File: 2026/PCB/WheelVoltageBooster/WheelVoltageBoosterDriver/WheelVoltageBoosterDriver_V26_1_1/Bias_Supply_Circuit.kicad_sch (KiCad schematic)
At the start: 27 parts, among them U1 MAX20405AFOA/VY+, U5 LD1117DT33CTR

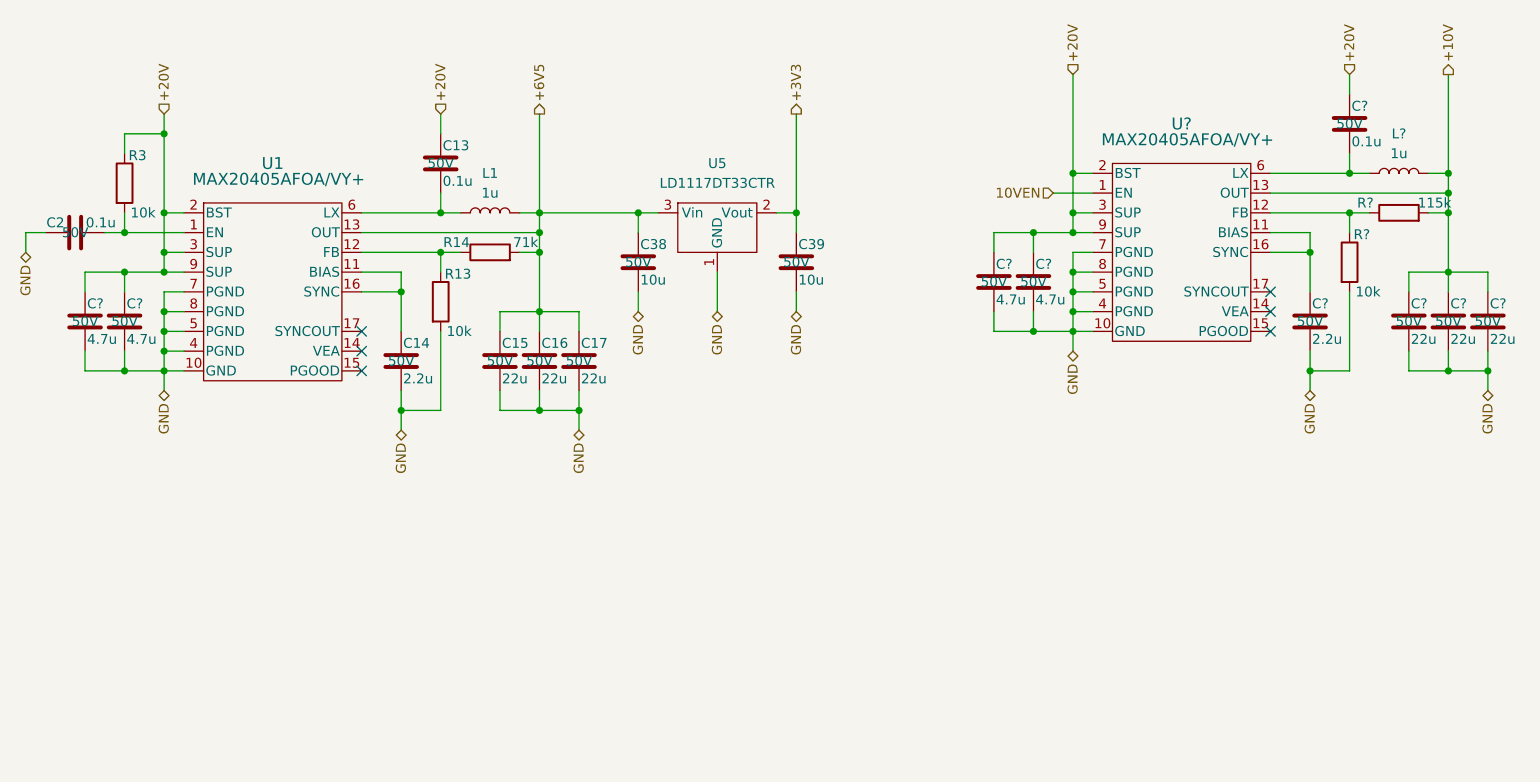
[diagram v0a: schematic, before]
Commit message: ５０V 測定用分圧抵抗追加
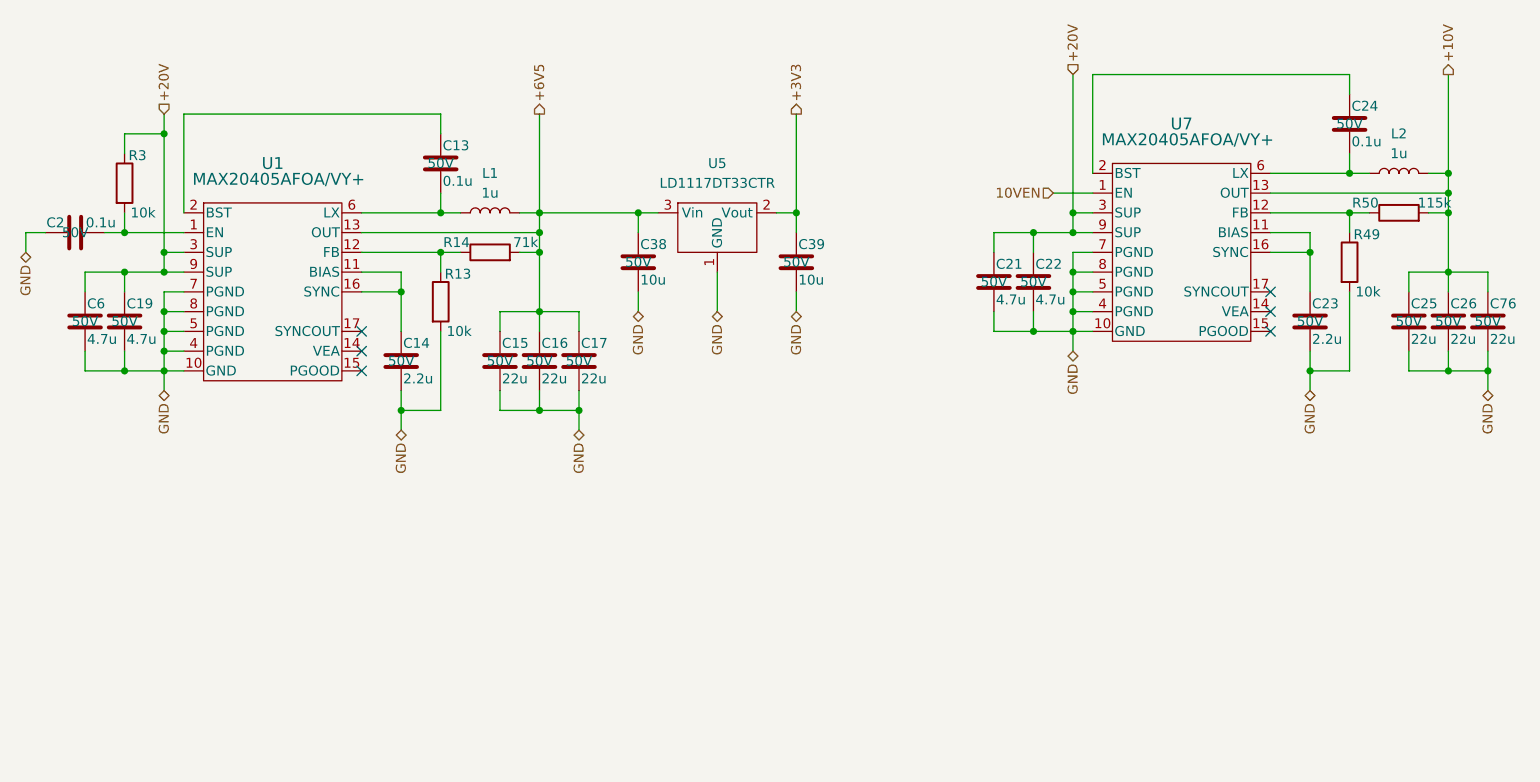
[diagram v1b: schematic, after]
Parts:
- gave numbers to parts that had none: 13
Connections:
- net +20V: no longer C13.1, C24.1, U1.2 (BST), U7.2 (BST)
- new net: C24.1, U7.2 (BST)
- new net: C13.1, U1.2 (BST)
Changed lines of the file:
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@@
 	)
 	(junction
-		(at 179.07 78.74)
-		(diameter 0)
-		(color 0 0 0 0)
-	)
-	(junction
 		(at 209.55 104.14)
 		(diameter 0)
@@
 	)
 	(junction
-		(at 62.23 83.82)
-		(diameter 0)
-		(color 0 0 0 0)
-	)
-	(junction
 		(at 227.33 81.28)
 		(diameter 0)
@@
 	(wire
 		(pts
-			(xy 179.07 66.04) (xy 179.07 78.74)
-		)
-		(stroke
-			(width 0)
-			(type default)
-		)
-	)
-	(wire
-		(pts
-			(xy 179.07 78.74) (xy 181.61 78.74)
-		)
-		(stroke
-			(width 0)
-			(type default)
-		)
-	)
-	(wire
-		(pts
 			(xy 115.57 106.68) (xy 115.57 109.22)
 		)
@@
 	(wire
 		(pts
-			(xy 179.07 78.74) (xy 179.07 83.82)
+			(xy 179.07 66.04) (xy 179.07 83.82)
 		)
 		(stroke
@@
 	(wire
 		(pts
+			(xy 181.61 66.04) (xy 214.63 66.04)
+		)
+		(stroke
+			(width 0)
+			(type default)
+		)
+	)
+	(wire
+		(pts
 			(xy 176.53 81.28) (xy 181.61 81.28)
 		)
@@
 	(wire
 		(pts
+			(xy 64.77 83.82) (xy 64.77 71.12)
+		)
+		(stroke
+			(width 0)
+			(type default)
+		)
+	)
+	(wire
+		(pts
 			(xy 110.49 83.82) (xy 123.19 83.82)
 		)
@@
 	(wire
 		(pts
-			(xy 62.23 83.82) (xy 64.77 83.82)
+			(xy 204.47 81.28) (xy 227.33 81.28)
 		)
 		(stroke
@@
 	(wire
 		(pts
-			(xy 204.47 81.28) (xy 227.33 81.28)
+			(xy 181.61 78.74) (xy 181.61 66.04)
 		)
 		(stroke
@@
 	(wire
 		(pts
-			(xy 62.23 83.82) (xy 62.23 88.9)
+			(xy 62.23 73.66) (xy 62.23 88.9)
 		)
 		(stroke
@@
 	(wire
 		(pts
-			(xy 52.07 93.98) (xy 52.07 91.44)
+			(xy 64.77 71.12) (xy 97.79 71.12)
 		)
 		(stroke
@@
 	(wire
 		(pts
-			(xy 227.33 78.74) (xy 224.79 78.74)
+			(xy 52.07 93.98) (xy 52.07 91.44)
 		)
 		(stroke
@@
 	(wire
 		(pts
-			(xy 179.07 93.98) (xy 179.07 91.44)
+			(xy 227.33 78.74) (xy 224.79 78.74)
 		)
 		(stroke
@@
 	(wire
 		(pts
-			(xy 123.19 83.82) (xy 123.19 86.36)
+			(xy 179.07 93.98) (xy 179.07 91.44)
 		)
 		(stroke
@@
 	(wire
 		(pts
-			(xy 140.97 83.82) (xy 143.51 83.82)
+			(xy 123.19 83.82) (xy 123.19 86.36)
 		)
 		(stroke
@@
 	(wire
 		(pts
-			(xy 62.23 73.66) (xy 62.23 83.82)
+			(xy 140.97 83.82) (xy 143.51 83.82)
 		)
 		(stroke
@@
 		)
 	)
-	(hierarchical_label "+20V"
-		(shape input)
-		(at 214.63 66.04 90)
-		(effects
-			(font
-				(size 1.27 1.27)
-			)
-			(justify left)
-		)
-	)
-	(hierarchical_label "+20V"
-		(shape input)
-		(at 97.79 71.12 90)
-		(effects
-			(font
-				(size 1.27 1.27)
-			)
-			(justify left)
-		)
-	)
 	(hierarchical_label "GND"
 		(shape bidirectional)
@@
 		(on_board yes)
 		(dnp no)
-		(property "Reference" "C?"
+		(property "Reference" "C25"
 			(at 222.504 95.504 0)
 			(effects
@@
 			(project "WheelVoltageBoosterDriver_V26_1_1"
 				(path "/80c9ed4f-d051-48b1-8382-19040773b73e/6c235b48-13ab-434e-8894-09a09ebdd0ec"
-					(reference "C?")
+					(reference "C25")
 					(unit 1)
 				)
@@
 		(on_board yes)
 		(dnp no)
-		(property "Reference" "R?"
+		(property "Reference" "R49"
 			(at 215.138 86.614 0)
 			(effects
@@
 			(project "WheelVoltageBoosterDriver_V26_1_1"
 				(path "/80c9ed4f-d051-48b1-8382-19040773b73e/6c235b48-13ab-434e-8894-09a09ebdd0ec"
-					(reference "R?")
+					(reference "R49")
 					(unit 1)
 				)
@@
 		(on_board yes)
 		(dnp no)
-		(property "Reference" "U?"
+		(property "Reference" "U7"
 			(at 193.04 72.39 0)
 			(effects
@@
 			(project "WheelVoltageBoosterDriver_V26_1_1"
 				(path "/80c9ed4f-d051-48b1-8382-19040773b73e/6c235b48-13ab-434e-8894-09a09ebdd0ec"
-					(reference "U?")
+					(reference "U7")
 					(unit 1)
 				)
@@
 		(dnp no)
 		(fields_autoplaced yes)
-		(property "Reference" "L?"
+		(property "Reference" "L2"
 			(at 220.98 73.66 90)
 			(effects
@@
 			(project "WheelVoltageBoosterDriver_V26_1_1"
 				(path "/80c9ed4f-d051-48b1-8382-19040773b73e/6c235b48-13ab-434e-8894-09a09ebdd0ec"
-					(reference "L?")
+					(reference "L2")
 					(unit 1)
 				)
@@
 		(on_board yes)
 		(dnp no)
-		(property "Reference" "C?"
+		(property "Reference" "C19"
 			(at 57.404 95.504 0)
 			(effects
@@
 			(project "WheelVoltageBoosterDriver_V26_1_1"
 				(path "/80c9ed4f-d051-48b1-8382-19040773b73e/6c235b48-13ab-434e-8894-09a09ebdd0ec"
-					(reference "C?")
+					(reference "C19")
 					(unit 1)
 				)
@@
 		(on_board yes)
 		(dnp no)
-		(property "Reference" "C?"
+		(property "Reference" "C24"
 			(at 214.884 70.104 0)
 			(effects
@@
 			(project "WheelVoltageBoosterDriver_V26_1_1"
 				(path "/80c9ed4f-d051-48b1-8382-19040773b73e/6c235b48-13ab-434e-8894-09a09ebdd0ec"
-					(reference "C?")
+					(reference "C24")
 					(unit 1)
 				)
@@
 		(on_board yes)
 		(dnp no)
-		(property "Reference" "C?"
+		(property "Reference" "C26"
 			(at 227.584 95.504 0)
 			(effects
@@
 			(project "WheelVoltageBoosterDriver_V26_1_1"
 				(path "/80c9ed4f-d051-48b1-8382-19040773b73e/6c235b48-13ab-434e-8894-09a09ebdd0ec"
-					(reference "C?")
+					(reference "C26")
 					(unit 1)
 				)
@@
 		(on_board yes)
 		(dnp no)
-		(property "Reference" "C?"
+		(property "Reference" "C22"
 			(at 174.244 90.424 0)
 			(effects
@@
 			(project "WheelVoltageBoosterDriver_V26_1_1"
 				(path "/80c9ed4f-d051-48b1-8382-19040773b73e/6c235b48-13ab-434e-8894-09a09ebdd0ec"
-					(reference "C?")
+					(reference "C22")
 					(unit 1)
 				)
@@
 		(on_board yes)
 		(dnp no)
-		(property "Reference" "R?"
+		(property "Reference" "R50"
 			(at 216.662 82.55 90)
 			(effects
@@
 			(project "WheelVoltageBoosterDriver_V26_1_1"
 				(path "/80c9ed4f-d051-48b1-8382-19040773b73e/6c235b48-13ab-434e-8894-09a09ebdd0ec"
-					(reference "R?")
+					(reference "R50")
 					(unit 1)
 				)
@@
 		(on_board yes)
 		(dnp no)
-		(property "Reference" "C?"
+		(property "Reference" "C23"
 			(at 209.804 95.504 0)
 			(effects
@@
 			(project "WheelVoltageBoosterDriver_V26_1_1"
 				(path "/80c9ed4f-d051-48b1-8382-19040773b73e/6c235b48-13ab-434e-8894-09a09ebdd0ec"
-					(reference "C?")
+					(reference "C23")
 					(unit 1)
 				)
@@
 		(on_board yes)
 		(dnp no)
-		(property "Reference" "C?"
+		(property "Reference" "C76"
 			(at 232.664 95.504 0)
 			(effects
@@
 			(project "WheelVoltageBoosterDriver_V26_1_1"
 				(path "/80c9ed4f-d051-48b1-8382-19040773b73e/6c235b48-13ab-434e-8894-09a09ebdd0ec"
-					(reference "C?")
+					(reference "C76")
 					(unit 1)
 				)
@@
 		(on_board yes)
 		(dnp no)
-		(property "Reference" "C?"
+		(property "Reference" "C6"
 			(at 52.324 95.504 0)
 			(effects
@@
 			(project "WheelVoltageBoosterDriver_V26_1_1"
 				(path "/80c9ed4f-d051-48b1-8382-19040773b73e/6c235b48-13ab-434e-8894-09a09ebdd0ec"
-					(reference "C?")
+					(reference "C6")
 					(unit 1)
 				)
@@
 		(on_board yes)
 		(dnp no)
-		(property "Reference" "C?"
+		(property "Reference" "C21"
 			(at 169.164 90.424 0)
 			(effects
@@
 			(project "WheelVoltageBoosterDriver_V26_1_1"
 				(path "/80c9ed4f-d051-48b1-8382-19040773b73e/6c235b48-13ab-434e-8894-09a09ebdd0ec"
-					(reference "C?")
+					(reference "C21")
 					(unit 1)
 				)

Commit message: 回路図完了
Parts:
- added D15, D16, D17: LED, symbol Device:LED
- added R60, R61, R62: 1k, symbol Device:R
- U5: renamed from U1; footprint 21-100343_F173A3FY+6_MXM -> (none)
- U7: footprint 21-100343_F173A3FY+6_MXM -> (none)
- renumbered C2 to C63, C6 to C64, C19 to C65, C14 to C66, C13 to C67, C15 to C68, C16 to C69, C17 to C70, C38 to C71, C39 to C72, C21 to C73, C22 to C74, C23 to C75, C24 to C76, C25 to C77, C26 to C78, C76 to C79, L1 to L3, L2 to L4, R3 to R59, R13 to R63, R14 to R64, R49 to R65, R50 to R66, U5 to U6
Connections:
- net +10V: now also R60.1
- net +3V3: now also R62.1
- net +6V5: now also R61.1
- net GND: now also D15.1 (K), D16.1 (K), D17.1 (K)
- new net: D16.2 (A), R61.2
- new net: D15.2 (A), R60.2
- new net: D17.2 (A), R62.2

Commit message: 部品紐付け途中
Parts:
- D15, D16, D17: footprint (none) -> WheelVoltageBooster_LIB_FTP:LED_1608_user_dif
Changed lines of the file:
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@@
 			)
 		)
-		(property "Footprint" ""
+		(property "Footprint" "WheelVoltageBooster_LIB_FTP:LED_1608_user_dif"
 			(at 68.58 139.7 0)
 			(effects
@@
 			)
 		)
-		(property "Footprint" ""
+		(property "Footprint" "WheelVoltageBooster_LIB_FTP:LED_1608_user_dif"
 			(at 68.58 133.35 0)
 			(effects
@@
 			)
 		)
-		(property "Footprint" ""
+		(property "Footprint" "WheelVoltageBooster_LIB_FTP:LED_1608_user_dif"
 			(at 68.58 146.05 0)
 			(effects

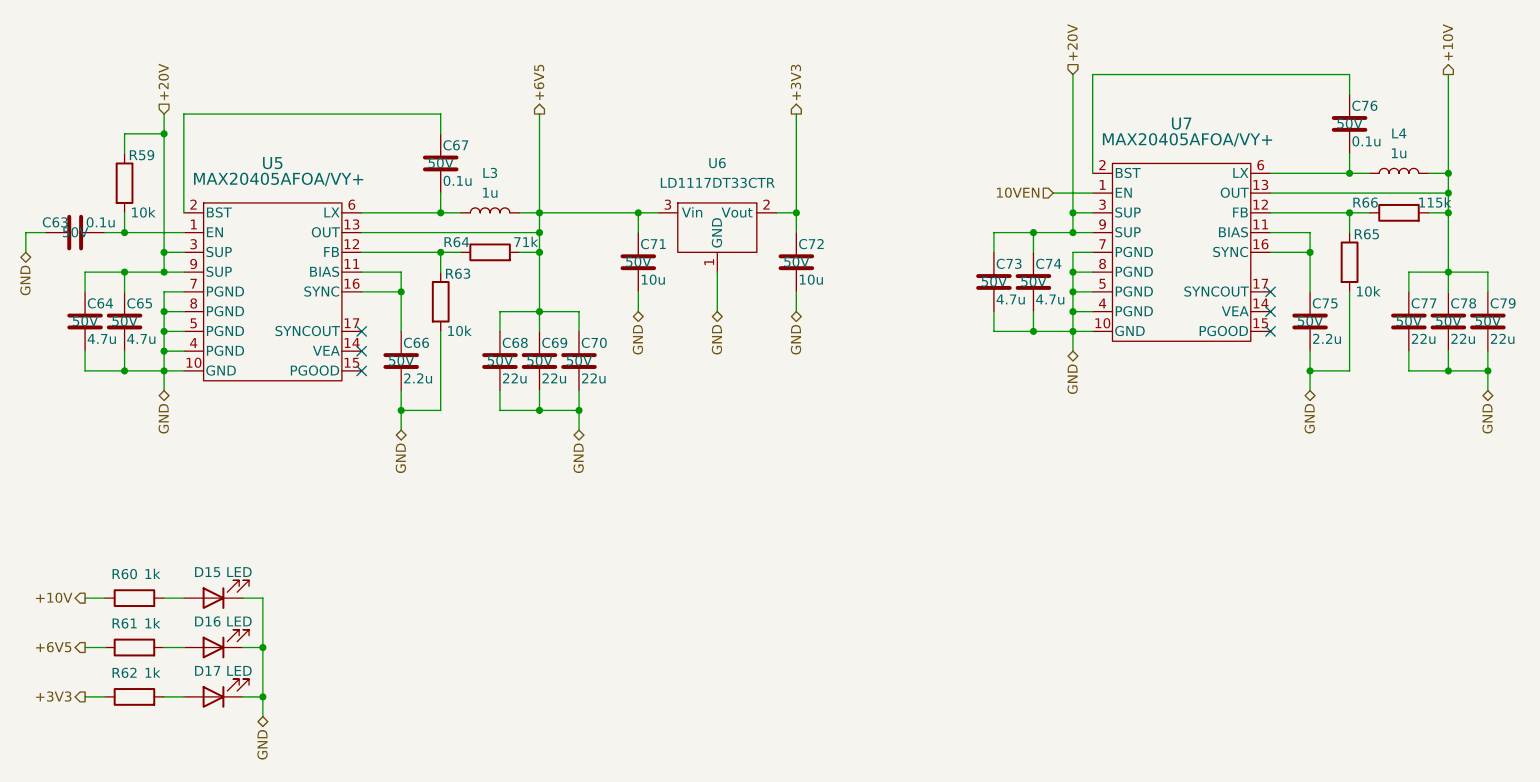
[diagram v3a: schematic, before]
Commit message: 回路再構築＆PCBに移行
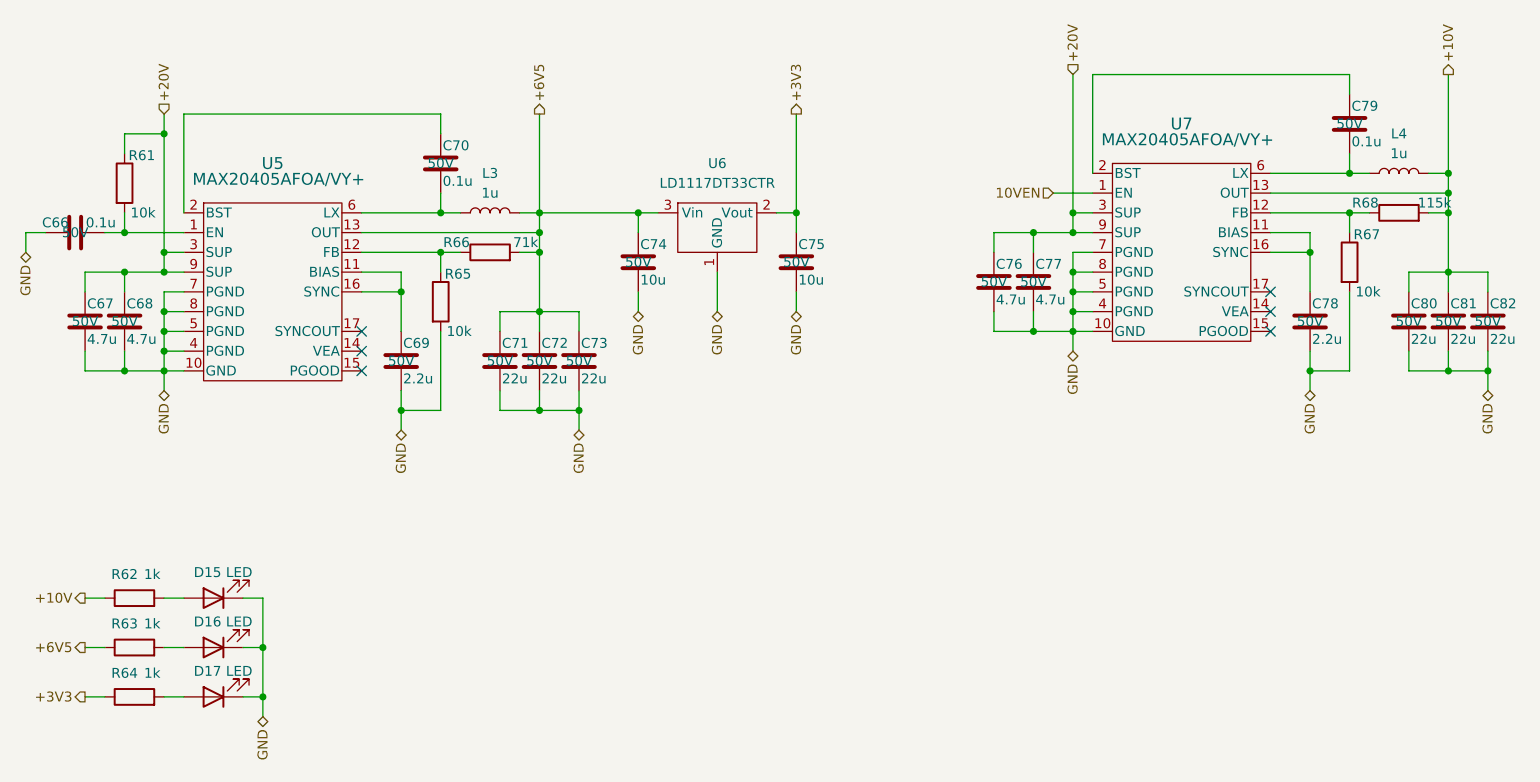
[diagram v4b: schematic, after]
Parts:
- C66: renamed from C63; footprint (none) -> Capacitor_SMD:C_0603_1608Metric_Pad1.08x0.95mm_HandSolder
- C67: renamed from C64; footprint (none) -> Capacitor_SMD:C_0805_2012Metric_Pad1.18x1.45mm_HandSolder
- C68: renamed from C65; footprint (none) -> Capacitor_SMD:C_0805_2012Metric_Pad1.18x1.45mm_HandSolder
- C69: renamed from C66; footprint (none) -> Capacitor_SMD:C_0603_1608Metric_Pad1.08x0.95mm_HandSolder
- C70: renamed from C67; footprint (none) -> Capacitor_SMD:C_0603_1608Metric_Pad1.08x0.95mm_HandSolder
- C71: renamed from C68; footprint (none) -> Capacitor_SMD:C_0603_1608Metric_Pad1.08x0.95mm_HandSolder
- C72: renamed from C69; footprint (none) -> Capacitor_SMD:C_0603_1608Metric_Pad1.08x0.95mm_HandSolder
- C73: renamed from C70; footprint (none) -> Capacitor_SMD:C_0603_1608Metric_Pad1.08x0.95mm_HandSolder
- C74: renamed from C71; footprint (none) -> Capacitor_SMD:C_0805_2012Metric_Pad1.18x1.45mm_HandSolder
- C75: renamed from C72; footprint (none) -> Capacitor_SMD:C_0805_2012Metric_Pad1.18x1.45mm_HandSolder
- C76: renamed from C73; footprint (none) -> Capacitor_SMD:C_0805_2012Metric_Pad1.18x1.45mm_HandSolder
- C77: renamed from C74; footprint (none) -> Capacitor_SMD:C_0805_2012Metric_Pad1.18x1.45mm_HandSolder
- C78: renamed from C75; footprint (none) -> Capacitor_SMD:C_0603_1608Metric_Pad1.08x0.95mm_HandSolder
- C79: renamed from C76; footprint (none) -> Capacitor_SMD:C_0603_1608Metric_Pad1.08x0.95mm_HandSolder
- C80: renamed from C77; footprint (none) -> Capacitor_SMD:C_0603_1608Metric_Pad1.08x0.95mm_HandSolder
- C81: renamed from C78; footprint (none) -> Capacitor_SMD:C_0603_1608Metric_Pad1.08x0.95mm_HandSolder
- C82: renamed from C79; footprint (none) -> Capacitor_SMD:C_0603_1608Metric_Pad1.08x0.95mm_HandSolder
- L3, L4: footprint (none) -> WheelVoltageBooster_LIB_FTP:74438366010
- R61: renamed from R59; footprint (none) -> Resistor_SMD:R_0402_1005Metric_Pad0.72x0.64mm_HandSolder
- R62: renamed from R60; footprint (none) -> Resistor_SMD:R_0402_1005Metric_Pad0.72x0.64mm_HandSolder
- R63: renamed from R61; footprint (none) -> Resistor_SMD:R_0402_1005Metric_Pad0.72x0.64mm_HandSolder
- R64: renamed from R62; footprint (none) -> Resistor_SMD:R_0402_1005Metric_Pad0.72x0.64mm_HandSolder
- R65: renamed from R63; footprint (none) -> Resistor_SMD:R_0402_1005Metric_Pad0.72x0.64mm_HandSolder
- R66: renamed from R64; footprint (none) -> Resistor_SMD:R_0402_1005Metric_Pad0.72x0.64mm_HandSolder
- R67: renamed from R65; footprint (none) -> Resistor_SMD:R_0402_1005Metric_Pad0.72x0.64mm_HandSolder
- R68: renamed from R66; footprint (none) -> Resistor_SMD:R_0402_1005Metric_Pad0.72x0.64mm_HandSolder
- U5, U7: footprint (none) -> WheelVoltageBooster_LIB_FTP:MAX20405AFOFVY
- U6: footprint (none) -> Package_TO_SOT_SMD:TO-252-2
